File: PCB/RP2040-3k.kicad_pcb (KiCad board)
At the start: 2 copper layers, 60 x 57 mm, 45 parts, among them J1 USB_C_Receptacle_USB2.0, SW1 MX_SW_HS, SW2 MX_SW_HS, SW3 MX_SW_HS, U1 RP2040, U2 SRV05-4, U3 XC6206PxxxMR, U4 W25Q16JVUXIQ, Y1 Crystal_GND24_Small

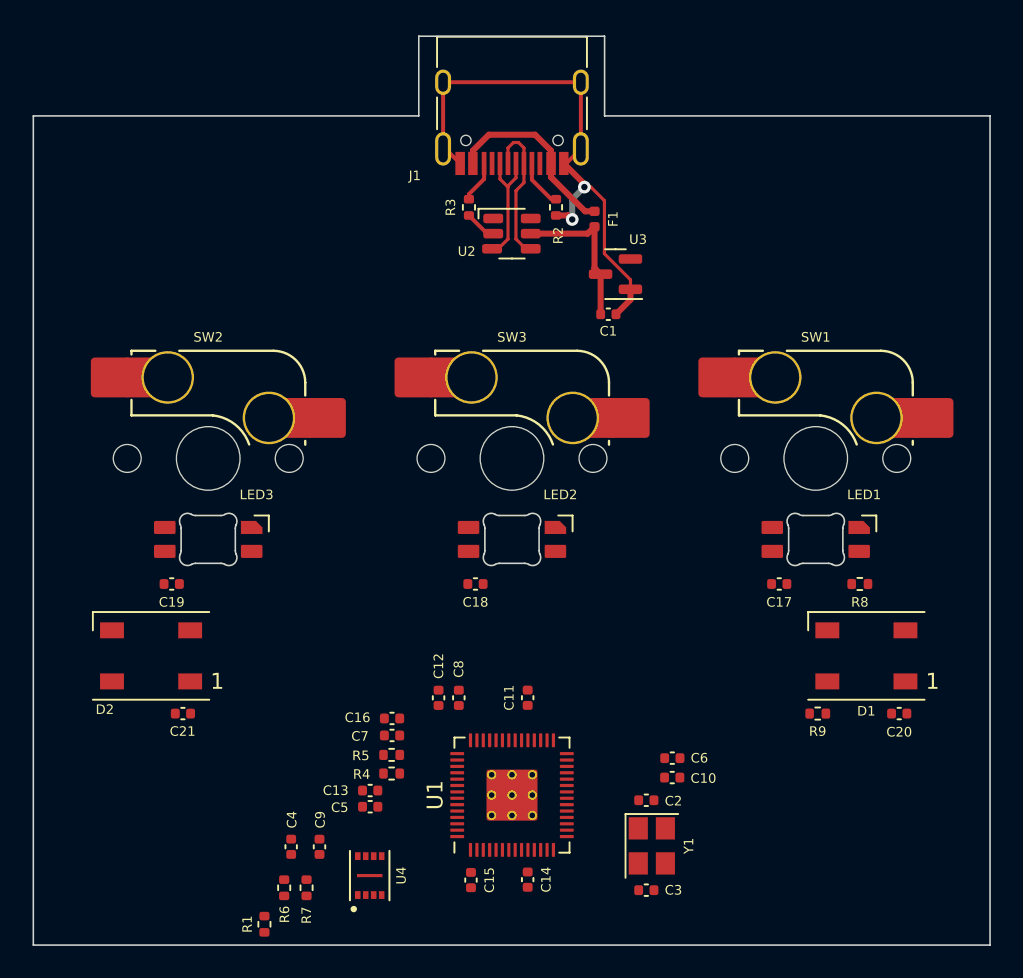
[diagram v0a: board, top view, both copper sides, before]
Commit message: Finished routing PCB
W25Q16JVUXIQTR library removed. Not using that part. Dimension changes made and other schematic things.
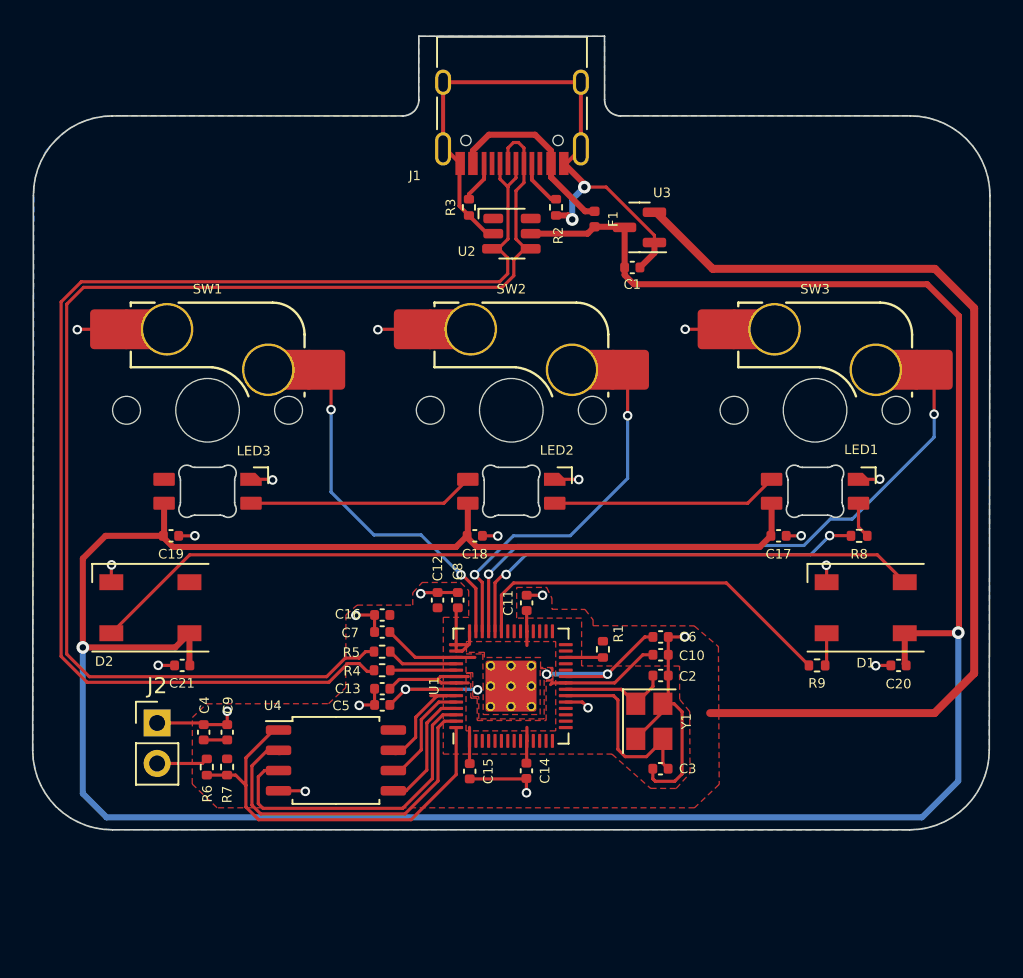
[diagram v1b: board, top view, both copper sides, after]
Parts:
- added J2: Conn_01x02, Connector_PinHeader_2.54mm:PinHeader_1x02_P2.54mm_Vertical, F.Cu at (61.1, 78.8)
- U4: value W25Q16JVUXIQ -> W25Q32JVSS; footprint W25Q16JVUXIQTR part:PSON50P300X200X60-9N -> Package_SO:SOIC-8_5.23x5.23mm_P1.27mm
- moved SW1 38.3 mm to (64.3, 59.2)
- moved R1 27.3 mm to (89.0, 74.2), turned to -90 degrees
- moved SW2 19.2 mm to (83.3, 59.2)
- moved SW3 19.2 mm to (102.4, 59.2)
- moved C9 9.22 mm to (65.5, 79.4)
- moved R7 9.07 mm to (65.5, 81.6)
- moved C4 9.04 mm to (64.0, 79.4)
- moved R6 8.99 mm to (64.2, 81.6)
- moved C2 7.87 mm to (92.7, 75.8)
- moved Y1 7.82 mm to (92.0, 78.7)
- moved C10 7.73 mm to (92.7, 74.5)
- moved C3 7.67 mm to (92.7, 81.7)
- moved C6 7.64 mm to (92.7, 73.4)
- moved U4 7.53 mm to (72.3, 81.2), turned to 0 degrees
- moved U1 6.84 mm to (83.3, 76.5)
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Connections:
- D1 pad 2: unconnected-(D1-Pad2) -> Net-(D1-Pad2)
- D2 pad 4: unconnected-(D2-Pad4) -> Net-(D1-Pad2)
- R6 pad 1: USB_BOOT -> /~{USB_BOOT}
- U1 pad 37: unconnected-(U1-Pad37) -> UNDERGLOW
- U1 pad 38: unconnected-(U1-Pad38) -> SWITCHLED
- U1 pad 39: unconnected-(U1-Pad39) -> COL2
- U1 pad 40: unconnected-(U1-Pad40) -> COL1
- U1 pad 41: unconnected-(U1-Pad41) -> COL0
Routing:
- net +5V: track 9.82 -> 197.2 mm, vias 0 -> 2
- net +3V3: track 0.00 -> 91.6 mm
- net D+: track 7.86 -> 82.1 mm
- net D-: track 9.35 -> 83.0 mm
- net GND: track 37.3 -> 93.7 mm, vias 2 -> 24
- net Net-(D1-Pad2): track 0.00 -> 52.5 mm
- net COL2: track 0.00 -> 39.5 mm, vias 0 -> 2
- net SWITCHLED: track 0.00 -> 26.6 mm, vias 0 -> 2
- net QSPI_SS: track 0.00 -> 26.2 mm
- net +1V1: track 0.00 -> 25.4 mm, vias 0 -> 4
- net UNDERGLOW: track 0.00 -> 24.0 mm
- net COL1: track 0.00 -> 22.7 mm, vias 0 -> 2
- net COL0: track 0.00 -> 22.1 mm, vias 0 -> 2
- net SD1: track 0.00 -> 22.0 mm
- net SD2: track 0.00 -> 20.0 mm
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- added copper zone on F.Cu, net +1V1
- added copper zone on F.Cu, net +3V3
- added copper zone on B.Cu, net GND
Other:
- board size 60 x 57 mm -> 60 x 49.8 mm
- board text added: "<- 1mm radius arc"
- board text added: "<- 5mm radius arc"

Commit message: Redid traces to tolerance
Clearance is now 0.2mm across the board. I also generated gerber files and etc
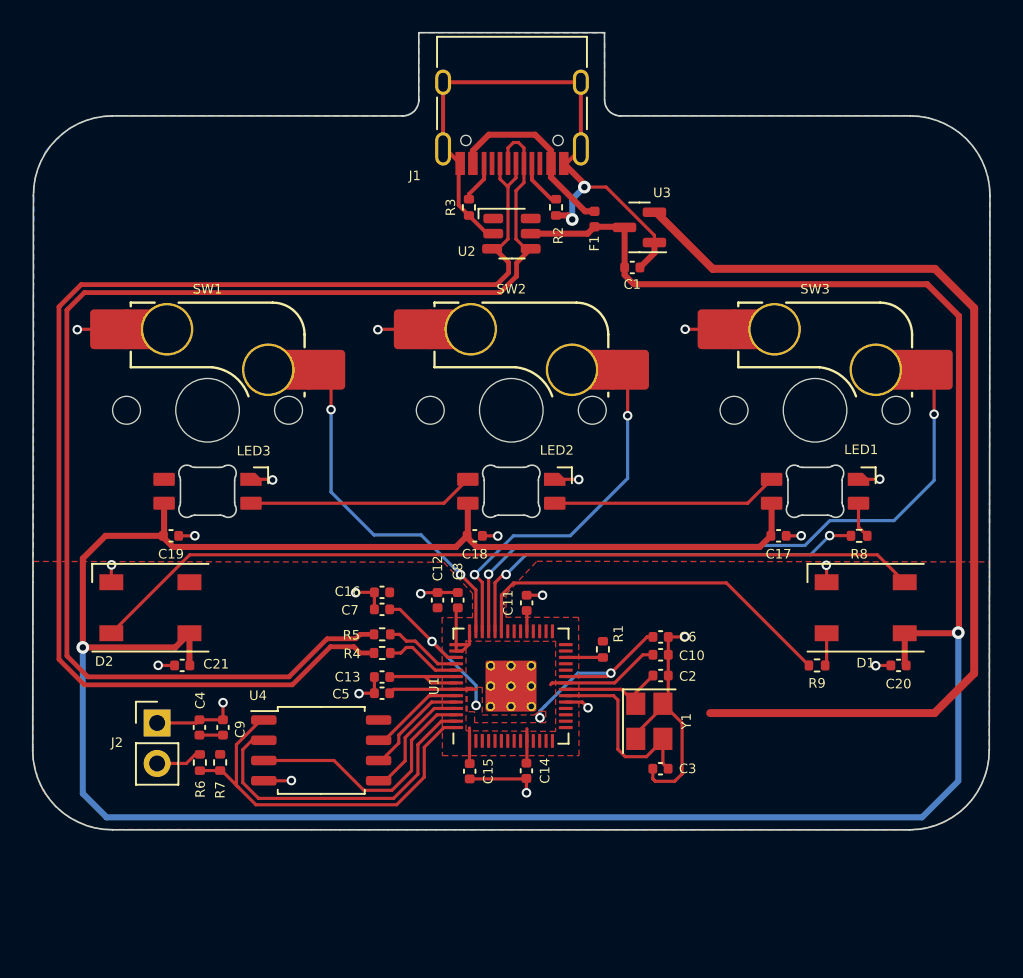
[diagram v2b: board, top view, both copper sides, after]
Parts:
- C2, C3: value 22p -> 5p
- moved C7 1.42 mm to (75.2, 71.7)
- moved C16 1.42 mm to (75.2, 70.6)
- moved U4 1.12 mm to (71.4, 80.5)
- moved R4 1.08 mm to (75.2, 74.4)
- moved R5 1.08 mm to (75.2, 73.3)
- moved C13 0.74 mm to (75.2, 75.9)
- moved C5 0.74 mm to (75.2, 77.0)
- moved R7 0.52 mm to (65.0, 81.3)
- moved R6 0.52 mm to (63.8, 81.3)
- moved C4 0.40 mm to (63.7, 79.1)
- moved C9 0.40 mm to (65.2, 79.1)
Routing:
- net SD2: track 20.0 -> 15.9 mm
- net +1V1: track 25.4 -> 28.5 mm
- net +3V3: track 91.6 -> 89.3 mm
- net SD1: track 22.0 -> 20.5 mm
- net COL2: track 39.5 -> 40.9 mm
- net SD3: track 7.19 -> 6.02 mm
- net QSPI_SS: track 26.2 -> 25.1 mm
- net D+: track 82.1 -> 83.1 mm
- net GND: track 93.7 -> 92.9 mm
- net Net-(R4-Pad1): track 4.13 -> 4.83 mm
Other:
- board size 60 x 49.8 mm -> 60 x 50 mm
- board text added: "tkkpad prototype 1.0"

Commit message: Fixed values and redid traces
Changed the data traces to be thicker. Redid crystal capacitor values (I originally calculated them wrongly). Changed 0.1uF values to 100nF for consistency. Regenerated BOM with updated changes
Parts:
- C1, C4: value 10u -> 20pF
- C17, C18, C19, C20, C21: value 0.1u -> 100n
- C2, C3: value 5p -> 10p
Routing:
- net GND: track 92.9 -> 95.2 mm, vias 24 -> 25
- net D+: track 83.1 -> 82.4 mm
- net D-: track 83.1 -> 83.7 mm

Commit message: Removed step up and fixed capacitor values
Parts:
- removed the R9 at (102.5, 75.2)
- added R7: 220, Resistor_SMD:R_0402_1005Metric, F.Cu at (102.4, 75.2)
- C2: renamed from C1; value 20pF -> 1uF
- C3: renamed from C4; value 20pF -> 1uF
- C4: renamed from C2; value 10p -> 20pF
- C5: renamed from C3; value 10p -> 20pF
- moved C3 44.1 mm to (94.2, 47.3), turned to -90 degrees
- moved C18 3.77 mm to (65.5, 72.7), turned to 90 degrees
- moved C10 0.61 mm to (64.7, 78.8), turned to 180 degrees
- moved R8 0.54 mm to (104.6, 67.1)
- moved C17 0.09 mm to (107.5, 75.2)
- renumbered C15 to C1, C9 to C10, C10 to C11, C11 to C12, C12 to C13, C13 to C14, C14 to C15, C20 to C17, C21 to C18, C17 to C19, C18 to C20, C19 to C21, C5 to C6, C6 to C7, C7 to C8, C8 to C9, R2 to R1, R7 to R2, R6 to R4, R4 to R5, R5 to R6, R1 to R9, U3 to U1, U4 to U3, U1 to U4
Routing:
- net +5V: track 197.2 -> 122.3 mm, vias 2 -> 4
- net +3V3: track 89.3 -> 102.9 mm, vias 0 -> 3
- net COL2: track 40.9 -> 37.8 mm, vias 2 -> 0
- net COL0: track 22.1 -> 20.3 mm, vias 2 -> 0
- net COL1: track 22.7 -> 21.6 mm, vias 2 -> 0
- net Net-(D1-Pad2): track 52.5 -> 53.4 mm, vias 0 -> 2
- net SWITCHLED: track 26.6 -> 26.0 mm, vias 2 -> 0
- net D-: track 83.7 -> 83.2 mm
- net GND: track 95.2 -> 95.3 mm, vias 25 -> 26
- net Net-(LED2-Pad2): track 14.2 -> 14.3 mm, vias 0 -> 2
- net Net-(LED1-Pad2): vias 0 -> 2
- added copper zone on F.Cu, net GND
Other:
- board text added: "tkkpad prototype 1.1"
- board text removed: "tkkpad prototype 1.0"
